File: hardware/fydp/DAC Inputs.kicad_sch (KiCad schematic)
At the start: 11 parts, among them J8 Conn_01x02_Pin, U1 LTC2630ISC6-LZ8-TRMPBF

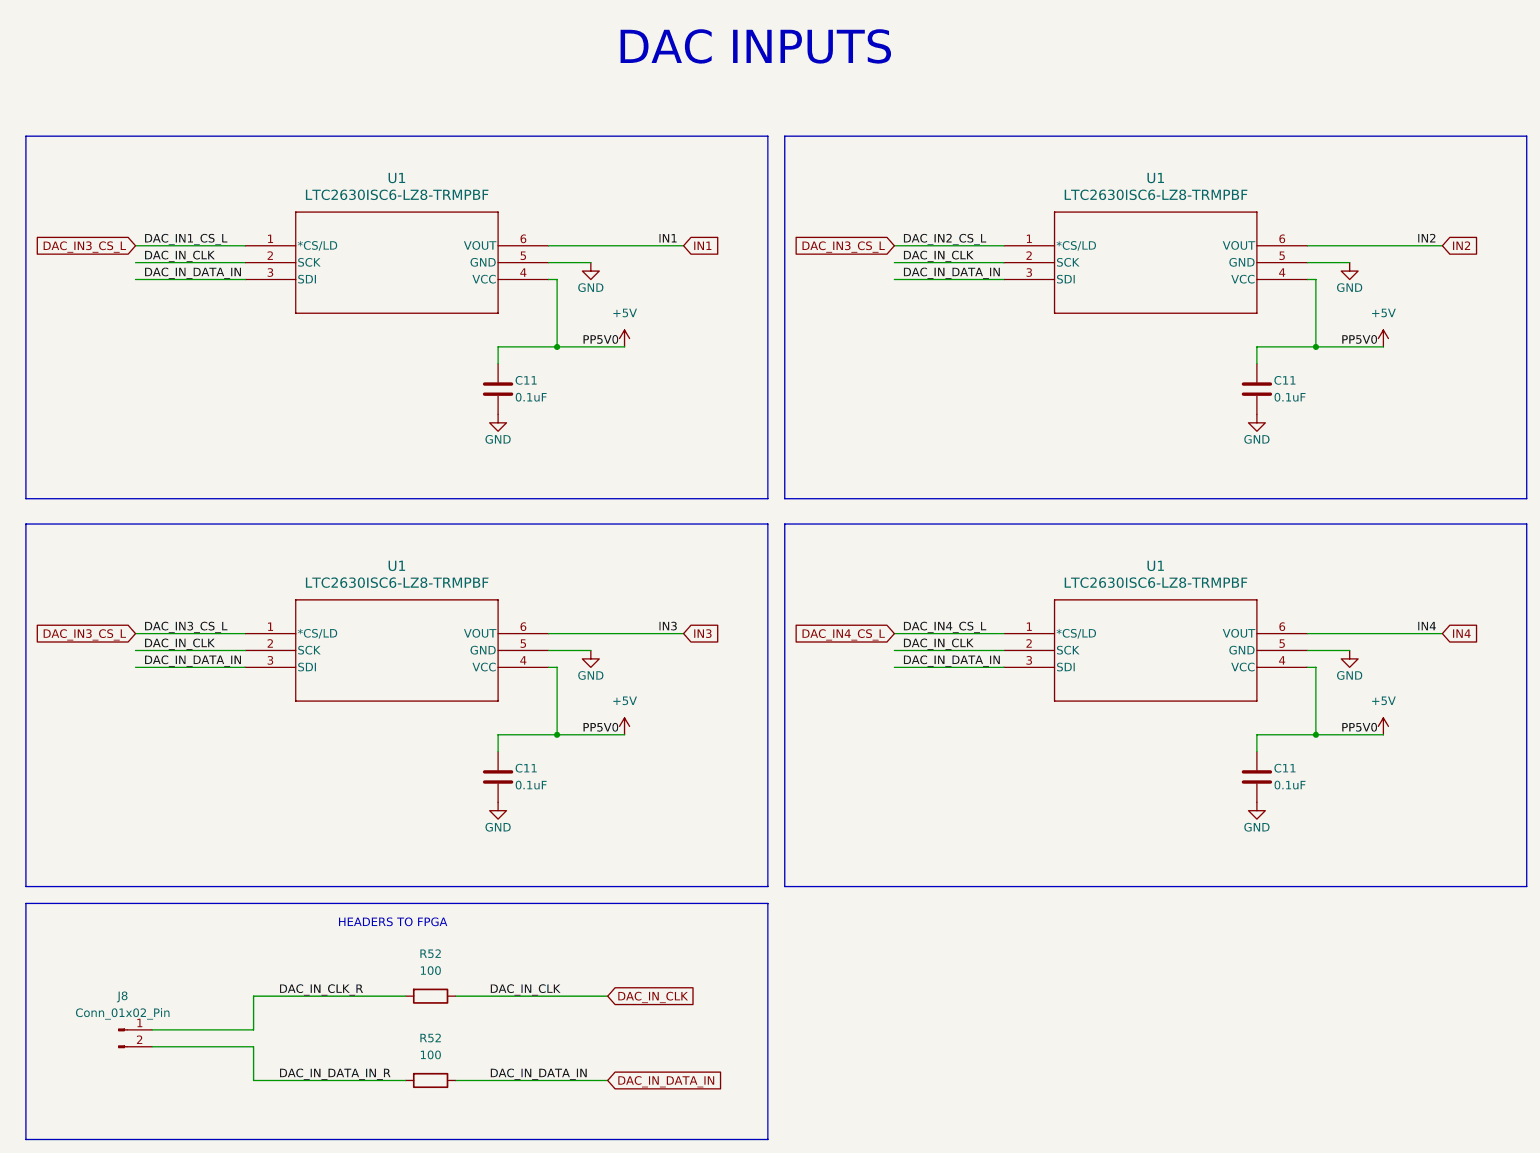
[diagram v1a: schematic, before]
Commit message: Completed placement and silk for left and centre sections of the PCB
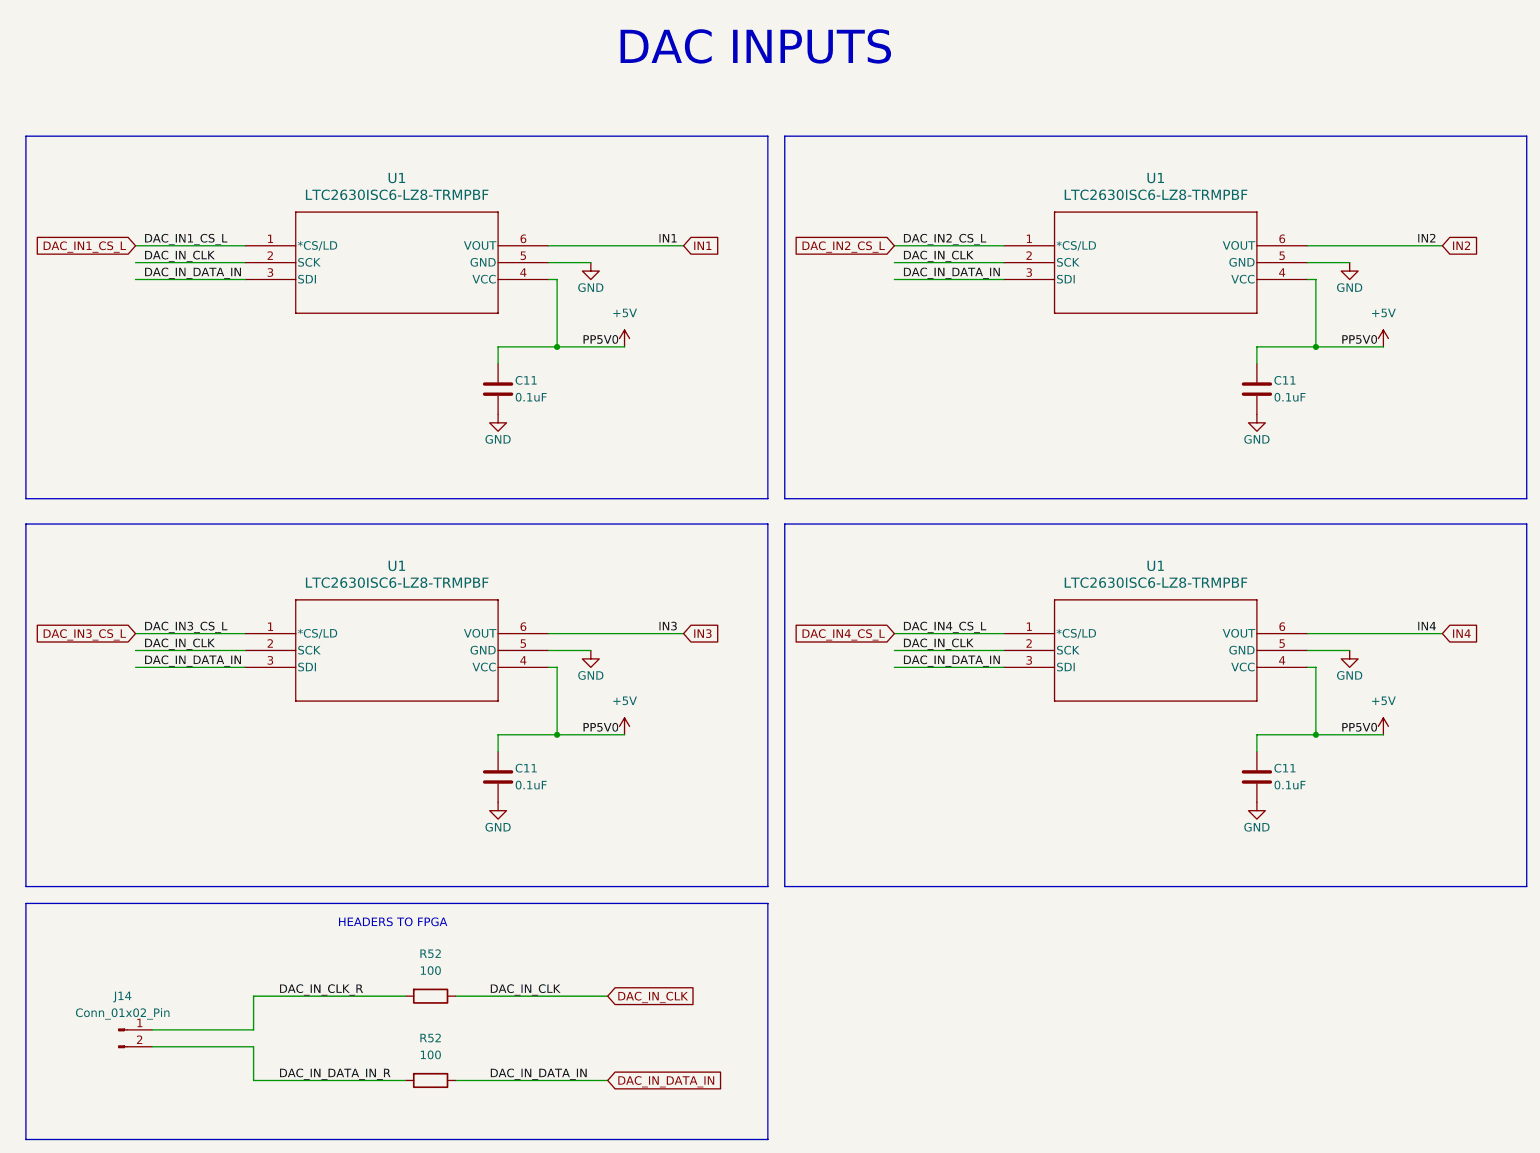
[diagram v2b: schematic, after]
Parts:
- renumbered J8 to J14
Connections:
- net DAC_IN3_CS_L: no longer U1.1 (*CS/LD), U1.1 (*CS/LD)
- new net DAC_IN1_CS_L: U1.1 (*CS/LD)
- new net DAC_IN2_CS_L: U1.1 (*CS/LD)
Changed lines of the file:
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@@
-    )
-  )
-  (global_label "DAC_IN3_CS_L" (shape input) (at 55.88 50.8 180) (fields_autoplaced)
-    (effects (font (size 1.27 1.27)) (justify right))
-    (property "Intersheetrefs" "${INTERSHEET_REFS}" (at 39.711 50.8 0)
-      (effects (font (size 1.27 1.27)) (justify right) hide)
     )
   )
@@
     )
   )
+  (global_label "DAC_IN2_CS_L" (shape input) (at 170.18 50.8 180) (fields_autoplaced)
+    (effects (font (size 1.27 1.27)) (justify right))
+    (property "Intersheetrefs" "${INTERSHEET_REFS}" (at 154.011 50.8 0)
+      (effects (font (size 1.27 1.27)) (justify right) hide)
+    )
+  )
+  (global_label "DAC_IN1_CS_L" (shape input) (at 55.88 50.8 180) (fields_autoplaced)
+    (effects (font (size 1.27 1.27)) (justify right))
+    (property "Intersheetrefs" "${INTERSHEET_REFS}" (at 39.711 50.8 0)
+      (effects (font (size 1.27 1.27)) (justify right) hide)
+    )
+  )
   (global_label "DAC_IN3_CS_L" (shape input) (at 55.88 109.22 180) (fields_autoplaced)
     (effects (font (size 1.27 1.27)) (justify right))
@@
     )
   )
-  (global_label "DAC_IN3_CS_L" (shape input) (at 170.18 50.8 180) (fields_autoplaced)
-    (effects (font (size 1.27 1.27)) (justify right))
-    (property "Intersheetrefs" "${INTERSHEET_REFS}" (at 154.011 50.8 0)
-      (effects (font (size 1.27 1.27)) (justify right) hide)
-    )
-  )
   (global_label "IN4" (shape input) (at 252.73 109.22 0) (fields_autoplaced)
     (effects (font (size 1.27 1.27)) (justify left))
@@
         )
         (path "/2d5d1aad-2c7d-465e-90ef-822dec61a05e/90317f24-347c-44df-9b72-f1982f583daa"
-          (reference "C194") (unit 1)
+          (reference "C19") (unit 1)
         )
       )
@@
         )
         (path "/2d5d1aad-2c7d-465e-90ef-822dec61a05e/90317f24-347c-44df-9b72-f1982f583daa"
-          (reference "#PWR0292") (unit 1)
+          (reference "#PWR064") (unit 1)
         )
       )
@@
         )
         (path "/2d5d1aad-2c7d-465e-90ef-822dec61a05e/90317f24-347c-44df-9b72-f1982f583daa"
-          (reference "C197") (unit 1)
+          (reference "C20") (unit 1)
         )
       )
@@
         )
         (path "/2d5d1aad-2c7d-465e-90ef-822dec61a05e/90317f24-347c-44df-9b72-f1982f583daa"
-          (reference "R78") (unit 1)
+          (reference "R57") (unit 1)
         )
       )
@@
         )
         (path "/2d5d1aad-2c7d-465e-90ef-822dec61a05e/90317f24-347c-44df-9b72-f1982f583daa"
-          (reference "#PWR0300") (unit 1)
+          (reference "#PWR070") (unit 1)
         )
       )
@@
         )
         (path "/2d5d1aad-2c7d-465e-90ef-822dec61a05e/90317f24-347c-44df-9b72-f1982f583daa"
-          (reference "#PWR041") (unit 1)
+          (reference "#PWR066") (unit 1)
         )
       )
@@
         )
         (path "/2d5d1aad-2c7d-465e-90ef-822dec61a05e/90317f24-347c-44df-9b72-f1982f583daa"
-          (reference "#PWR0296") (unit 1)
+          (reference "#PWR065") (unit 1)
         )
       )
@@
         )
         (path "/2d5d1aad-2c7d-465e-90ef-822dec61a05e/90317f24-347c-44df-9b72-f1982f583daa"
-          (reference "U52") (unit 1)
+          (reference "U9") (unit 1)
         )
       )
@@
         )
         (path "/2d5d1aad-2c7d-465e-90ef-822dec61a05e/90317f24-347c-44df-9b72-f1982f583daa"
-          (reference "#PWR0302") (unit 1)
+          (reference "#PWR075") (unit 1)
         )
       )
@@
         )
         (path "/2d5d1aad-2c7d-465e-90ef-822dec61a05e/90317f24-347c-44df-9b72-f1982f583daa"
-          (reference "U51") (unit 1)
+          (reference "U8") (unit 1)
         )
       )
@@
         )
         (path "/2d5d1aad-2c7d-465e-90ef-822dec61a05e/90317f24-347c-44df-9b72-f1982f583daa"
-          (reference "#PWR049") (unit 1)
+          (reference "#PWR073") (unit 1)
         )
       )
@@
         )
         (path "/2d5d1aad-2c7d-465e-90ef-822dec61a05e/90317f24-347c-44df-9b72-f1982f583daa"
-          (reference "#PWR0290") (unit 1)
+          (reference "#PWR068") (unit 1)
         )
       )
@@
         )
         (path "/2d5d1aad-2c7d-465e-90ef-822dec61a05e/90317f24-347c-44df-9b72-f1982f583daa"
-          (reference "#PWR0294") (unit 1)
+          (reference "#PWR069") (unit 1)
         )
       )
@@
         )
         (path "/2d5d1aad-2c7d-465e-90ef-822dec61a05e/90317f24-347c-44df-9b72-f1982f583daa"
-          (reference "C200") (unit 1)
+          (reference "C21") (unit 1)
         )
       )
@@
         )
         (path "/2d5d1aad-2c7d-465e-90ef-822dec61a05e/90317f24-347c-44df-9b72-f1982f583daa"
-          (reference "U50") (unit 1)
+          (reference "U7") (unit 1)
         )
       )
@@
   (symbol (lib_id "Connector:Conn_01x02_Pin") (at 53.34 168.91 0) (unit 1)
     (in_bom yes) (on_board yes) (dnp no)
-    (property "Reference" "J8" (at 53.975 163.83 0)
+    (property "Reference" "J14" (at 53.975 163.83 0)
       (effects (font (size 1.27 1.27)))
     )
@@
       (project "fydp"
         (path "/2d5d1aad-2c7d-465e-90ef-822dec61a05e/90317f24-347c-44df-9b72-f1982f583daa"
-          (reference "J8") (unit 1)
+          (reference "J14") (unit 1)
         )
         (path "/2d5d1aad-2c7d-465e-90ef-822dec61a05e/252f6ad9-45e0-4005-acd7-c69776b48ba5"
@@
         )
         (path "/2d5d1aad-2c7d-465e-90ef-822dec61a05e/90317f24-347c-44df-9b72-f1982f583daa"
-          (reference "R77") (unit 1)
+          (reference "R56") (unit 1)
         )
       )
@@
         )
         (path "/2d5d1aad-2c7d-465e-90ef-822dec61a05e/90317f24-347c-44df-9b72-f1982f583daa"
-          (reference "#PWR0304") (unit 1)
+          (reference "#PWR071") (unit 1)
         )
       )
@@
         )
         (path "/2d5d1aad-2c7d-465e-90ef-822dec61a05e/90317f24-347c-44df-9b72-f1982f583daa"
-          (reference "#PWR0298") (unit 1)
+          (reference "#PWR074") (unit 1)
         )
       )
@@
         )
         (path "/2d5d1aad-2c7d-465e-90ef-822dec61a05e/90317f24-347c-44df-9b72-f1982f583daa"
-          (reference "#PWR050") (unit 1)
+          (reference "#PWR072") (unit 1)
         )
       )
@@
         )
         (path "/2d5d1aad-2c7d-465e-90ef-822dec61a05e/90317f24-347c-44df-9b72-f1982f583daa"
-          (reference "#PWR042") (unit 1)
+          (reference "#PWR067") (unit 1)
         )
       )
@@
         )
         (path "/2d5d1aad-2c7d-465e-90ef-822dec61a05e/90317f24-347c-44df-9b72-f1982f583daa"
-          (reference "U49") (unit 1)
+          (reference "U6") (unit 1)
         )
       )
@@
         )
         (path "/2d5d1aad-2c7d-465e-90ef-822dec61a05e/90317f24-347c-44df-9b72-f1982f583daa"
-          (reference "C203") (unit 1)
-        )
-      )
+          (reference "C22") (unit 1)
+        )
+      )

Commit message: Adding JLCPCB BOM notes
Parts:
- C11: Comment (none) -> 0.1 µF ±10% 50V Ceramic Capacitor X7R 0805 (2012 Metric); LCSC (none) -> C49678; MPN (none) -> CC0805KRX7R9BB104
- R52: Comment (none) -> 100 Ohms ±1% 0.125W, 1/8W Chip Resistor 0805 (2012 Metric) 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; LCSC (none) -> C105577; MPN (none) -> RC0805FR-07100RL
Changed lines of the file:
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@@
       (effects (font (size 1.27 1.27)) hide)
     )
-    (property "Datasheet" "~" (at 110.49 72.39 0)
+    (property "Datasheet" "https://www.yageo.com/upload/media/product/app/datasheet/mlcc/upy-gphc_x7r_6_3v-to-250v.pdf" (at 110.49 72.39 0)
+      (effects (font (size 1.27 1.27)) hide)
+    )
+    (property "Comment" "0.1 µF ±10% 50V Ceramic Capacitor X7R 0805 (2012 Metric)" (at 110.49 72.39 0)
+      (effects (font (size 1.27 1.27)) hide)
+    )
+    (property "LCSC" "C49678" (at 110.49 72.39 0)
+      (effects (font (size 1.27 1.27)) hide)
+    )
+    (property "MPN" "CC0805KRX7R9BB104" (at 110.49 72.39 0)
       (effects (font (size 1.27 1.27)) hide)
     )
@@
       (effects (font (size 1.27 1.27)) hide)
     )
-    (property "Datasheet" "~" (at 224.79 72.39 0)
+    (property "Datasheet" "https://www.yageo.com/upload/media/product/app/datasheet/mlcc/upy-gphc_x7r_6_3v-to-250v.pdf" (at 224.79 72.39 0)
+      (effects (font (size 1.27 1.27)) hide)
+    )
+    (property "Comment" "0.1 µF ±10% 50V Ceramic Capacitor X7R 0805 (2012 Metric)" (at 224.79 72.39 0)
+      (effects (font (size 1.27 1.27)) hide)
+    )
+    (property "LCSC" "C49678" (at 224.79 72.39 0)
+      (effects (font (size 1.27 1.27)) hide)
+    )
+    (property "MPN" "CC0805KRX7R9BB104" (at 224.79 72.39 0)
       (effects (font (size 1.27 1.27)) hide)
     )
@@
       (effects (font (size 1.27 1.27)) hide)
     )
-    (property "Datasheet" "~" (at 100.33 176.53 0)
+    (property "Datasheet" "https://www.yageo.com/upload/media/product/products/datasheet/rchip/PYu-RC_Group_51_RoHS_L_12.pdf" (at 100.33 176.53 0)
+      (effects (font (size 1.27 1.27)) hide)
+    )
+    (property "Comment" "100 Ohms ±1% 0.125W, 1/8W Chip Resistor 0805 (2012 Metric) Moisture Resistant Thick Film" (at 100.33 176.53 0)
+      (effects (font (size 1.27 1.27)) hide)
+    )
+    (property "LCSC" "C105577" (at 100.33 176.53 0)
+      (effects (font (size 1.27 1.27)) hide)
+    )
+    (property "MPN" "RC0805FR-07100RL" (at 100.33 176.53 0)
       (effects (font (size 1.27 1.27)) hide)
     )
@@
       (effects (font (size 1.27 1.27)) hide)
     )
-    (property "Datasheet" "~" (at 110.49 130.81 0)
+    (property "Datasheet" "https://www.yageo.com/upload/media/product/app/datasheet/mlcc/upy-gphc_x7r_6_3v-to-250v.pdf" (at 110.49 130.81 0)
+      (effects (font (size 1.27 1.27)) hide)
+    )
+    (property "Comment" "0.1 µF ±10% 50V Ceramic Capacitor X7R 0805 (2012 Metric)" (at 110.49 130.81 0)
+      (effects (font (size 1.27 1.27)) hide)
+    )
+    (property "LCSC" "C49678" (at 110.49 130.81 0)
+      (effects (font (size 1.27 1.27)) hide)
+    )
+    (property "MPN" "CC0805KRX7R9BB104" (at 110.49 130.81 0)
       (effects (font (size 1.27 1.27)) hide)
     )
@@
       (effects (font (size 1.27 1.27)) hide)
     )
-    (property "Datasheet" "~" (at 100.33 163.83 0)
+    (property "Datasheet" "https://www.yageo.com/upload/media/product/products/datasheet/rchip/PYu-RC_Group_51_RoHS_L_12.pdf" (at 100.33 163.83 0)
+      (effects (font (size 1.27 1.27)) hide)
+    )
+    (property "Comment" "100 Ohms ±1% 0.125W, 1/8W Chip Resistor 0805 (2012 Metric) Moisture Resistant Thick Film" (at 100.33 163.83 0)
+      (effects (font (size 1.27 1.27)) hide)
+    )
+    (property "LCSC" "C105577" (at 100.33 163.83 0)
+      (effects (font (size 1.27 1.27)) hide)
+    )
+    (property "MPN" "RC0805FR-07100RL" (at 100.33 163.83 0)
       (effects (font (size 1.27 1.27)) hide)
     )
@@
       (effects (font (size 1.27 1.27)) hide)
     )
-    (property "Datasheet" "~" (at 224.79 130.81 0)
-      (effects (font (size 1.27 1.27)) hide)
-    )
+    (property "Datasheet" "https://www.yageo.com/upload/media/product/app/datasheet/mlcc/upy-gphc_x7r_6_3v-to-250v.pdf" (at 224.79 130.81 0)
+      (effects (font (size 1.27 1.27)) hide)
+    )
+    (property "Comment" "0.1 µF ±10% 50V Ceramic Capacitor X7R 0805 (2012 Metric)" (at 224.79 130.81 0)
+      (effects (font (size 1.27 1.27)) hide)
+    )
+    (property "LCSC" "C49678" (at 224.79 130.81 0)
+      (effects (font (size 1.27 1.27)) hide)
+    )
+    (property "MPN" "CC0805KRX7R9BB104" (at 224.79 130.81 0)
+      (effects (font (size 1.27 1.27)) hide)
+    )

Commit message: Updating BOM some more
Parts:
- J14: Comment (none) -> Connector Header Through Hole 2 position 0.100" (2.54mm); MPN (none) -> TSW-102-07-G-S
- U1: Comment (none) -> 8 Bit Digital to Analog Converter 1 SC-70-6; MPN (none) -> LTC2630ISC6-LZ8#TRMPBF
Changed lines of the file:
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@@
       (effects (font (size 1.27 1.27) italic) hide)
     )
-    (property "Datasheet" "LTC2630ISC6-LZ8-TRMPBF" (at 186.69 109.22 0)
-      (effects (font (size 1.27 1.27) italic) hide)
+    (property "Datasheet" "https://www.analog.com/media/en/technical-documentation/data-sheets/2630fg.pdf" (at 186.69 109.22 0)
+      (effects (font (size 1.27 1.27) italic) hide)
+    )
+    (property "Comment" "8 Bit Digital to Analog Converter 1 SC-70-6" (at 186.69 109.22 0)
+      (effects (font (size 1.27 1.27)) hide)
+    )
+    (property "MPN" "LTC2630ISC6-LZ8#TRMPBF" (at 186.69 109.22 0)
+      (effects (font (size 1.27 1.27)) hide)
     )
     (pin "1")
@@
       (effects (font (size 1.27 1.27) italic) hide)
     )
-    (property "Datasheet" "LTC2630ISC6-LZ8-TRMPBF" (at 72.39 109.22 0)
-      (effects (font (size 1.27 1.27) italic) hide)
+    (property "Datasheet" "https://www.analog.com/media/en/technical-documentation/data-sheets/2630fg.pdf" (at 72.39 109.22 0)
+      (effects (font (size 1.27 1.27) italic) hide)
+    )
+    (property "Comment" "8 Bit Digital to Analog Converter 1 SC-70-6" (at 72.39 109.22 0)
+      (effects (font (size 1.27 1.27)) hide)
+    )
+    (property "MPN" "LTC2630ISC6-LZ8#TRMPBF" (at 72.39 109.22 0)
+      (effects (font (size 1.27 1.27)) hide)
     )
     (pin "1")
@@
       (effects (font (size 1.27 1.27) italic) hide)
     )
-    (property "Datasheet" "LTC2630ISC6-LZ8-TRMPBF" (at 186.69 50.8 0)
-      (effects (font (size 1.27 1.27) italic) hide)
+    (property "Datasheet" "https://www.analog.com/media/en/technical-documentation/data-sheets/2630fg.pdf" (at 186.69 50.8 0)
+      (effects (font (size 1.27 1.27) italic) hide)
+    )
+    (property "Comment" "8 Bit Digital to Analog Converter 1 SC-70-6" (at 186.69 50.8 0)
+      (effects (font (size 1.27 1.27)) hide)
+    )
+    (property "MPN" "LTC2630ISC6-LZ8#TRMPBF" (at 186.69 50.8 0)
+      (effects (font (size 1.27 1.27)) hide)
     )
     (pin "1")
@@
       (effects (font (size 1.27 1.27)) hide)
     )
-    (property "Datasheet" "~" (at 53.34 168.91 0)
+    (property "Datasheet" "https://suddendocs.samtec.com/catalog_english/tsw_th.pdf" (at 53.34 168.91 0)
+      (effects (font (size 1.27 1.27)) hide)
+    )
+    (property "Comment" "Connector Header Through Hole 2 position 0.100\" (2.54mm)" (at 53.34 168.91 0)
+      (effects (font (size 1.27 1.27)) hide)
+    )
+    (property "MPN" "TSW-102-07-G-S" (at 53.34 168.91 0)
       (effects (font (size 1.27 1.27)) hide)
     )
@@
       (effects (font (size 1.27 1.27) italic) hide)
     )
-    (property "Datasheet" "LTC2630ISC6-LZ8-TRMPBF" (at 72.39 50.8 0)
-      (effects (font (size 1.27 1.27) italic) hide)
-    )
-    (pin "1")
+    (property "Datasheet" "https://www.analog.com/media/en/technical-documentation/data-sheets/2630fg.pdf" (at 72.39 50.8 0)
+      (effects (font (size 1.27 1.27) italic) hide)
+    )
+    (property "Comment" "8 Bit Digital to Analog Converter 1 SC-70-6" (at 72.39 50.8 0)
+      (effects (font (size 1.27 1.27)) hide)
+    )
+    (property "MPN" "LTC2630ISC6-LZ8#TRMPBF" (at 72.39 50.8 0)
+      (effects (font (size 1.27 1.27)) hide)
+    )
+    (pin "1")
